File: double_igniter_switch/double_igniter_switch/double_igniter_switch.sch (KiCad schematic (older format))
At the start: 20 parts, among them J1 Speaker_terminal, J2 Conn_02x04_Odd_Even, Q1 IPD50N06S4L-12, Q2 IPD50N06S4L-12, U1 MCP1416, U2 MCP1416

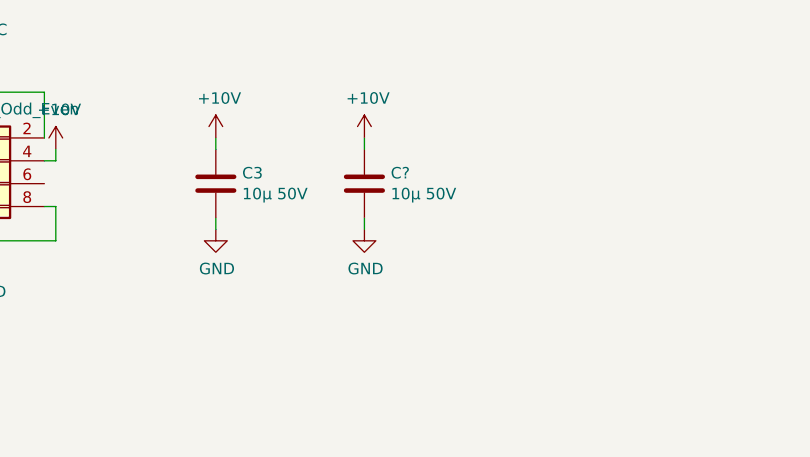
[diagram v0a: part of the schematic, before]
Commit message: added expander board with layout
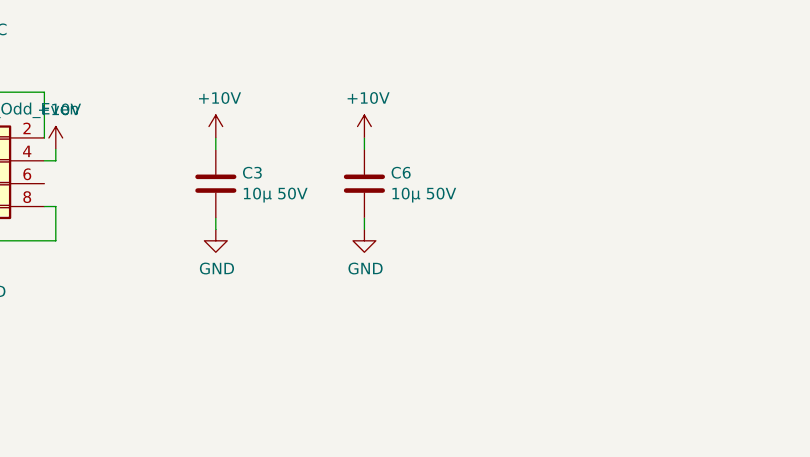
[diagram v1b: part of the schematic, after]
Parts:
- gave numbers to parts that had none: 1
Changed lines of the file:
@@
 EESchema Schematic File Version 4
-LIBS:double_igniter_switch-cache
 EELAYER 26 0
 EELAYER END
@@
 	1700 2050 2000 2050
 $Comp
-L Device:C C?
+L Device:C C6
 U 1 1 5D884236
 P 5600 2100
-F 0 "C?" H 5715 2146 50  0000 L CNN
+F 0 "C6" H 5715 2146 50  0000 L CNN
 F 1 "10µ 50V" H 5715 2055 50  0000 L CNN
 F 2 "Capacitor_SMD:C_1206_3216Metric" H 5638 1950 50  0001 C CNN
@@
 	5600 1950 5600 1900
 $Comp
-L power:GND #PWR?
+L power:GND #PWR0101
 U 1 1 5D88423F
 P 5600 2300
-F 0 "#PWR?" H 5600 2050 50  0001 C CNN
+F 0 "#PWR0101" H 5600 2050 50  0001 C CNN
 F 1 "GND" H 5605 2127 50  0000 C CNN
 F 2 "" H 5600 2300 50  0001 C CNN
@@
 $EndComp
 $Comp
-L power:+10V #PWR?
+L power:+10V #PWR0102
 U 1 1 5D884245
 P 5600 1900
-F 0 "#PWR?" H 5600 1750 50  0001 C CNN
+F 0 "#PWR0102" H 5600 1750 50  0001 C CNN
 F 1 "+10V" H 5615 2073 50  0000 C CNN
 F 2 "" H 5600 1900 50  0001 C CNN

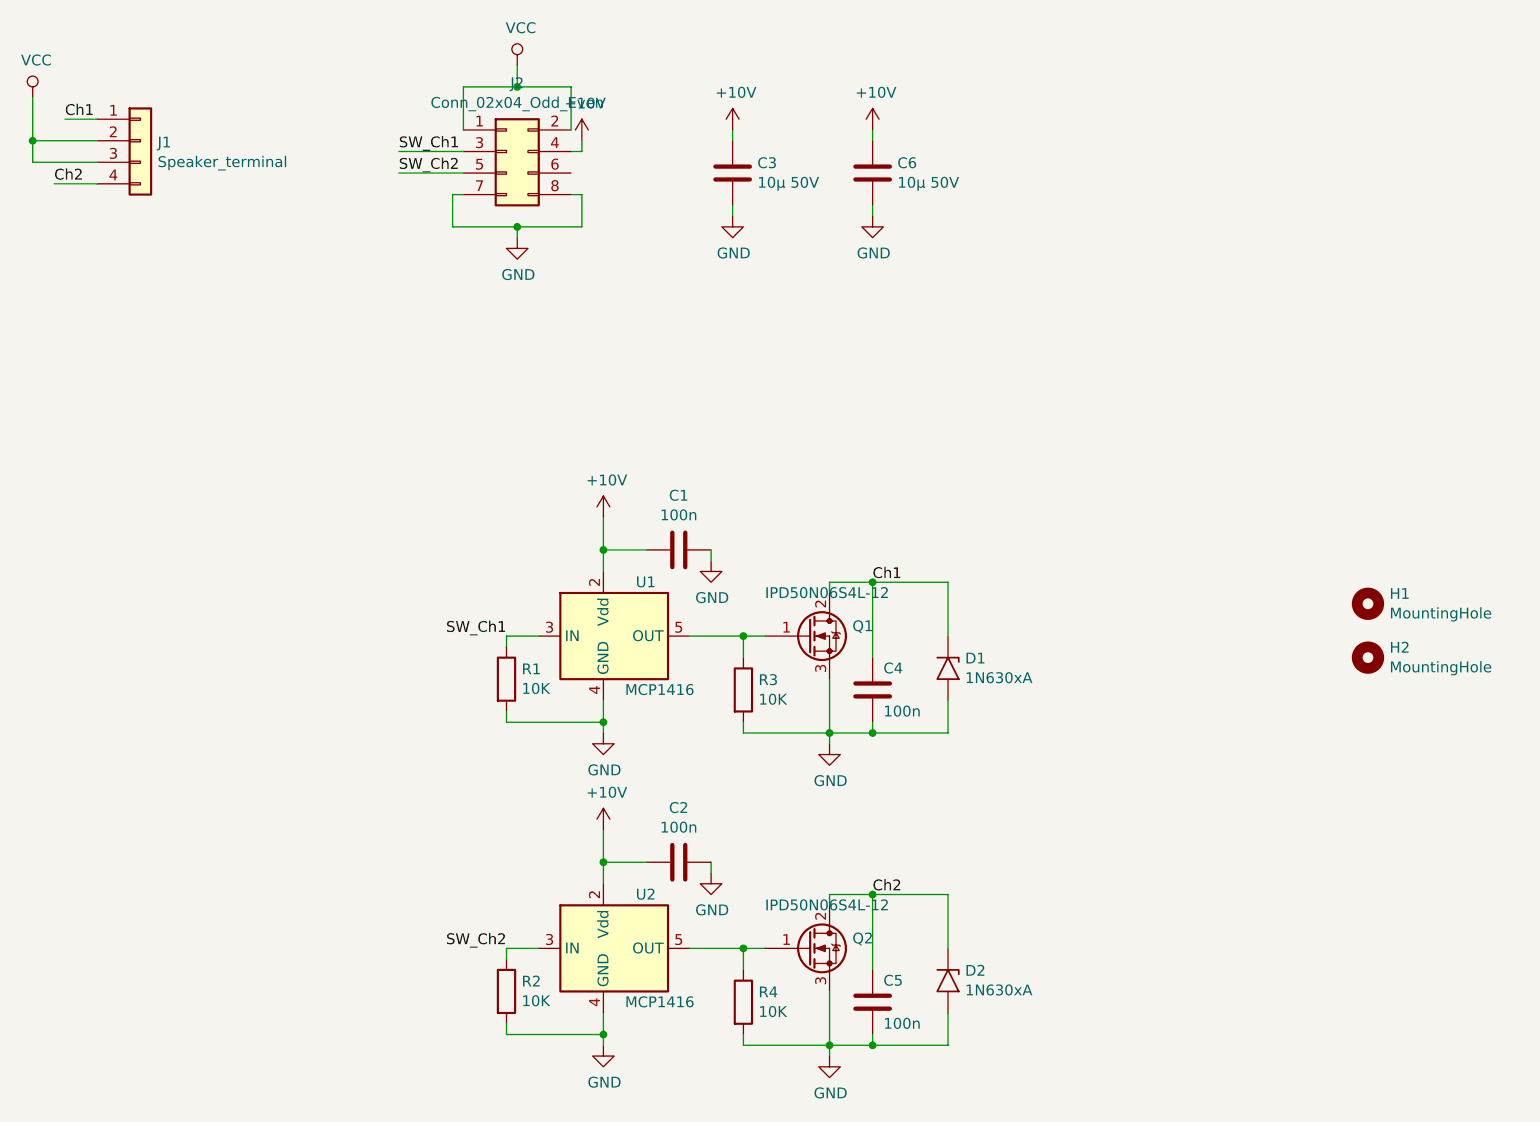
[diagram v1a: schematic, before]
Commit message: added esd diode and free wheeling dioed to mosfet module, removed gate drive, changed pinout
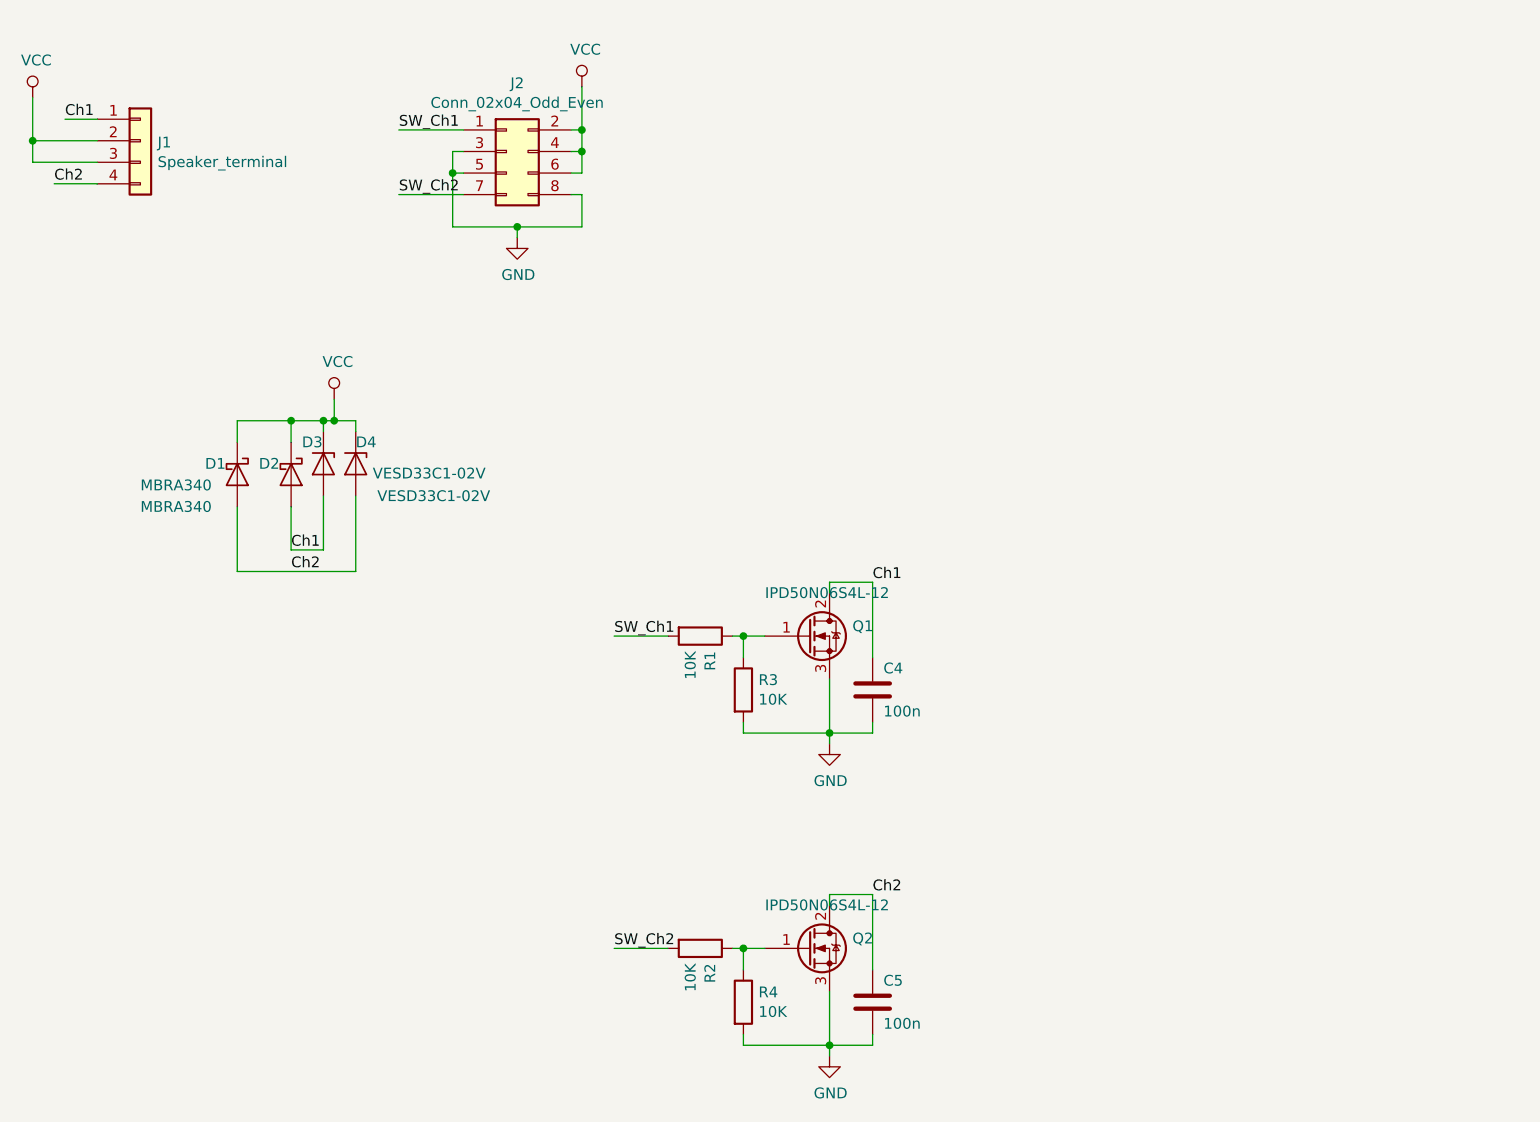
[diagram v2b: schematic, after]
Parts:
- removed C1, C2: 100n, Capacitor_SMD:C_0603_1608Metric, symbol Device:C
- removed C3, C6: 10µ 50V, Capacitor_SMD:C_1206_3216Metric, symbol Device:C
- removed D1, D2: 1N630xA, Diode_THT:D_DO-201AE_P15.24mm_Horizontal, symbol Diode:1N630xA
- removed H1, H2: MountingHole, MountingHole:MountingHole_3.2mm_M3, symbol Mechanical:MountingHole
- removed U1, U2: MCP1416, Package_TO_SOT_SMD:SOT-23-5, symbol Driver_FET:MCP1416
- added D1, D2: MBRA340, Diode_SMD:D_SMA, symbol Device:D_Schottky
- added D3, D4: VESD33C1-02V, Diode_SMD:D_SOD-523, symbol Device:D_Zener
- C4, C5: footprint Capacitor_SMD:C_0603_1608Metric -> Resistor_SMD:R_1206_3216Metric
- R1, R2, R3, R4: footprint Resistor_SMD:R_0603_1608Metric -> Resistor_SMD:R_1206_3216Metric
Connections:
- net +10V is gone; now on net VCC: J2.4 (Pin_4)
- net Ch1: now also D2.2 (A), D3.2 (A)
- net Ch2: now also D1.2 (A), D4.2 (A)
- net GND: now also J2.3 (Pin_3), J2.5 (Pin_5); no longer J2.7 (Pin_7), R1.2, R2.2
- net SW_Ch1: now also J2.1 (Pin_1), R1.2; no longer J2.3 (Pin_3), R1.1
- net SW_Ch2: now also J2.7 (Pin_7), R2.2; no longer J2.5 (Pin_5), R2.1
- net VCC: now also J2.6 (Pin_6), D1.1 (K), D2.1 (K), D3.1 (K), D4.1 (K); no longer J2.1 (Pin_1)
- net at Q1.1 (G), R3.1: now also R1.1
- net at Q2.1 (G), R4.1: now also R2.1
